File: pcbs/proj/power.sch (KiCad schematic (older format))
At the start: 23 parts, among them J4 Conn_02x05_Odd_Even, J5 Barrel_Jack, U34 TS30011/12/13

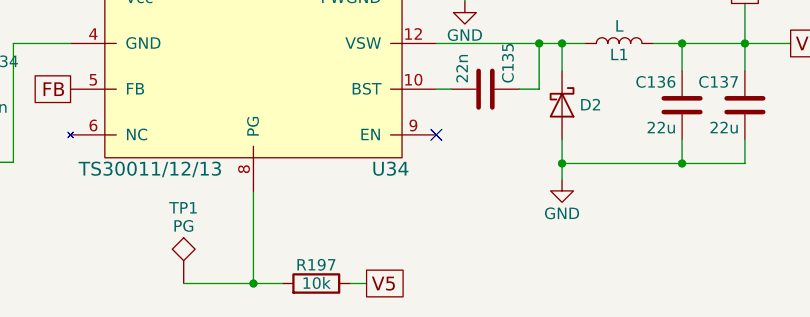
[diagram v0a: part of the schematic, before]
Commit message: All components placed.
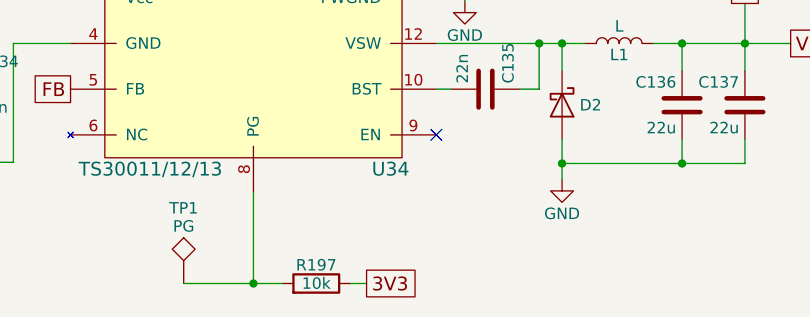
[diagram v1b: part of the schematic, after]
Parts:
- C135, C136, C137: footprint Resistors_SMD:R_0805 -> Resistors_SMD:R_0603
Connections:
- net 3V3: now also R197.1
- net FB: no longer R197.1
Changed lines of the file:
@@
 $EndComp
 $Comp
-L GND #PWR0324
+L GND #PWR0292
 U 1 1 5A0AD8CE
 P 5090 3180
-F 0 "#PWR0324" H 5090 2930 50  0001 C CNN
+F 0 "#PWR0292" H 5090 2930 50  0001 C CNN
 F 1 "GND" H 5090 3030 50  0000 C CNN
 F 2 "" H 5090 3180 50  0001 C CNN
@@
 F 0 "C136" H 5665 5715 50  0000 L CNN
 F 1 "22u" H 5665 5515 50  0000 L CNN
-F 2 "Resistors_SMD:R_0805" H 5678 5465 50  0001 C CNN
+F 2 "Resistors_SMD:R_0603" H 5678 5465 50  0001 C CNN
 F 3 "https://media.digikey.com/pdf/Data%20Sheets/Samsung%20PDFs/CL21A226MQCLQNC_character.pdf" H 5640 5615 50  0001 C CNN
 F 4 "1276-2412-1-ND" H 5640 5615 60  0001 C CNN "Digikey"
@@
 F 0 "C137" H 5940 5715 50  0000 L CNN
 F 1 "22u" H 5940 5515 50  0000 L CNN
-F 2 "Resistors_SMD:R_0805" H 5953 5465 50  0001 C CNN
+F 2 "Resistors_SMD:R_0603" H 5953 5465 50  0001 C CNN
 F 3 "https://media.digikey.com/pdf/Data%20Sheets/Samsung%20PDFs/CL21A226MQCLQNC_character.pdf" H 5915 5615 50  0001 C CNN
 F 4 "1276-2412-1-ND" H 5915 5615 60  0001 C CNN "Digikey"
@@
 F 0 "C135" H 4805 5645 50  0000 L CNN
 F 1 "22n" H 4805 5445 50  0000 L CNN
-F 2 "Resistors_SMD:R_0805" H 4818 5395 50  0001 C CNN
+F 2 "Resistors_SMD:R_0603" H 4818 5395 50  0001 C CNN
 F 3 "" H 4780 5545 50  0001 C CNN
 F 4 "1276-1104-1-ND" H 4780 5545 60  0001 C CNN "Digikey"
@@
 V18
 $Comp
-L GND #PWR0325
+L GND #PWR0293
 U 1 1 5A0B8173
 P 5115 5940
-F 0 "#PWR0325" H 5115 5690 50  0001 C CNN
+F 0 "#PWR0293" H 5115 5690 50  0001 C CNN
 F 1 "GND" H 5115 5790 50  0000 C CNN
 F 2 "" H 5115 5940 50  0001 C CNN
@@
 FB
 $Comp
-L GND #PWR0326
+L GND #PWR0294
 U 1 1 5A0B8CE5
 P 4690 5160
-F 0 "#PWR0326" H 4690 4910 50  0001 C CNN
+F 0 "#PWR0294" H 4690 4910 50  0001 C CNN
 F 1 "GND" H 4690 5010 50  0000 C CNN
 F 2 "" H 4690 5160 50  0001 C CNN
@@
 $EndComp
 $Comp
-L GND #PWR0327
+L GND #PWR0295
 U 1 1 5A0BC4D5
 P 1985 5940
-F 0 "#PWR0327" H 1985 5690 50  0001 C CNN
+F 0 "#PWR0295" H 1985 5690 50  0001 C CNN
 F 1 "GND" H 1985 5790 50  0000 C CNN
 F 2 "" H 1985 5940 50  0001 C CNN
@@
 $EndComp
 Text GLabel 4260 6395 2    60   UnSpc ~ 0
-V5
+3V3
 $Comp
 L LED D4
@@
 $EndComp
 $Comp
-L GND #PWR0328
+L GND #PWR0296
 U 1 1 5A0C1EE8
 P 8770 4770
-F 0 "#PWR0328" H 8770 4520 50  0001 C CNN
+F 0 "#PWR0296" H 8770 4520 50  0001 C CNN
 F 1 "GND" H 8770 4620 50  0000 C CNN
 F 2 "" H 8770 4770 50  0001 C CNN
@@
 $EndComp
 $Comp
-L GND #PWR0329
+L GND #PWR0297
 U 1 1 5A0EF3E8
 P 8740 2900
-F 0 "#PWR0329" H 8740 2650 50  0001 C CNN
+F 0 "#PWR0297" H 8740 2650 50  0001 C CNN
 F 1 "GND" H 8740 2750 50  0000 C CNN
 F 2 "" H 8740 2900 50  0001 C CNN
@@
 3V3
 $Comp
-L PWR_FLAG #FLG0330
+L PWR_FLAG #FLG0298
 U 1 1 5A107991
 P 5025 3960
-F 0 "#FLG0330" H 5025 4035 50  0001 C CNN
+F 0 "#FLG0298" H 5025 4035 50  0001 C CNN
 F 1 "PWR_FLAG" H 5025 4110 50  0000 C CNN
 F 2 "" H 5025 3960 50  0001 C CNN
@@
 V18
 $Comp
-L PWR_FLAG #FLG0331
+L PWR_FLAG #FLG0299
 U 1 1 5A107A22
 P 5475 3960
-F 0 "#FLG0331" H 5475 4035 50  0001 C CNN
+F 0 "#FLG0299" H 5475 4035 50  0001 C CNN
 F 1 "PWR_FLAG" H 5475 4110 50  0000 C CNN
 F 2 "" H 5475 3960 50  0001 C CNN

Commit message: Some progress layouting the beast today.
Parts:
- R198: footprint Resistors_SMD:R_1206 -> Resistors_SMD:R_2512_HandSoldering
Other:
- note added: "Current Rating (IPC 2221)\n----------------------\nMax. Expected Current = 64 * 0.05 A = 3.2 A \nAbs. Max. Current (dT = 10 K, W = 1.6 mm) = 3.36 A"
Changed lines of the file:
@@
 F 0 "R198" V 4890 2410 50  0000 C CNN
 F 1 "0R" V 4810 2410 50  0000 C CNN
-F 2 "Resistors_SMD:R_1206" V 4740 2410 50  0001 C CNN
+F 2 "Resistors_SMD:R_2512_HandSoldering" V 4740 2410 50  0001 C CNN
 F 3 "" H 4810 2410 50  0001 C CNN
 F 4 "311-0.0ERCT-ND" V 4810 2410 60  0001 C CNN "Digikey"
@@
 Text Notes 4830 3720 0    60   ~ 0
 Tell Kicad, that these voltages are externally driven.
+Text Notes 4060 1605 0    60   ~ 0
+Current Rating (IPC 2221)\n----------------------\nMax. Expected Current = 64 * 0.05 A = 3.2 A \nAbs. Max. Current (dT = 10 K, W = 1.6 mm) = 3.36 A
 $EndSCHEMATC

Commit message: Started eliminating DRC errors.
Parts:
- R198: footprint Resistors_SMD:R_2512_HandSoldering -> Resistors_SMD:R_1206
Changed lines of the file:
@@
 F 0 "R198" V 4890 2410 50  0000 C CNN
 F 1 "0R" V 4810 2410 50  0000 C CNN
-F 2 "Resistors_SMD:R_2512_HandSoldering" V 4740 2410 50  0001 C CNN
+F 2 "Resistors_SMD:R_1206" V 4740 2410 50  0001 C CNN
 F 3 "" H 4810 2410 50  0001 C CNN
 F 4 "311-0.0ERCT-ND" V 4810 2410 60  0001 C CNN "Digikey"
